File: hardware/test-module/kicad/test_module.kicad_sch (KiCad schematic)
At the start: 14 parts, among them J1 Barrel_Jack_12V, M1 ERM_Motor, M2 Stepper_4wire, M3 Servo_3pin, U1 D24V22F5_Buck, U2 Pi_Pico_W, U3 DRV2605L_Breakout, U4 DRV8871_Breakout, U5 Tic_T500

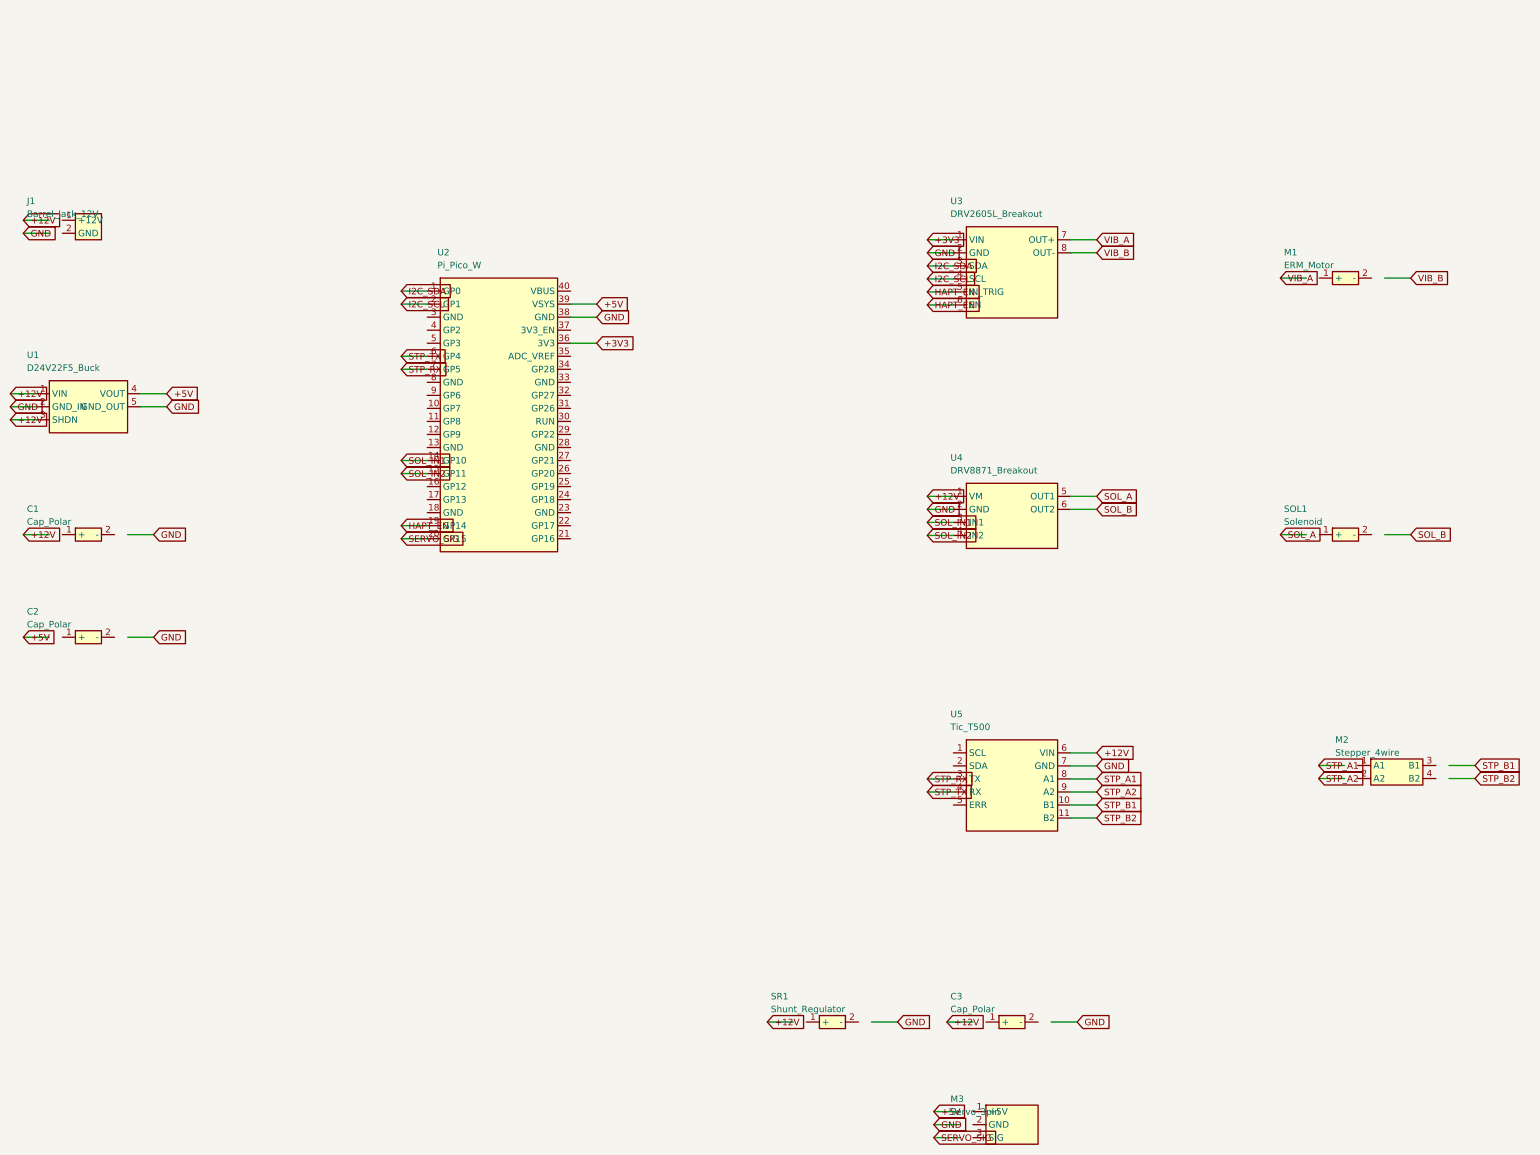
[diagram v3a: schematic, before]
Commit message: Add dual-servo dispensing-angle control (unison, mirrored) to firmware + schematic
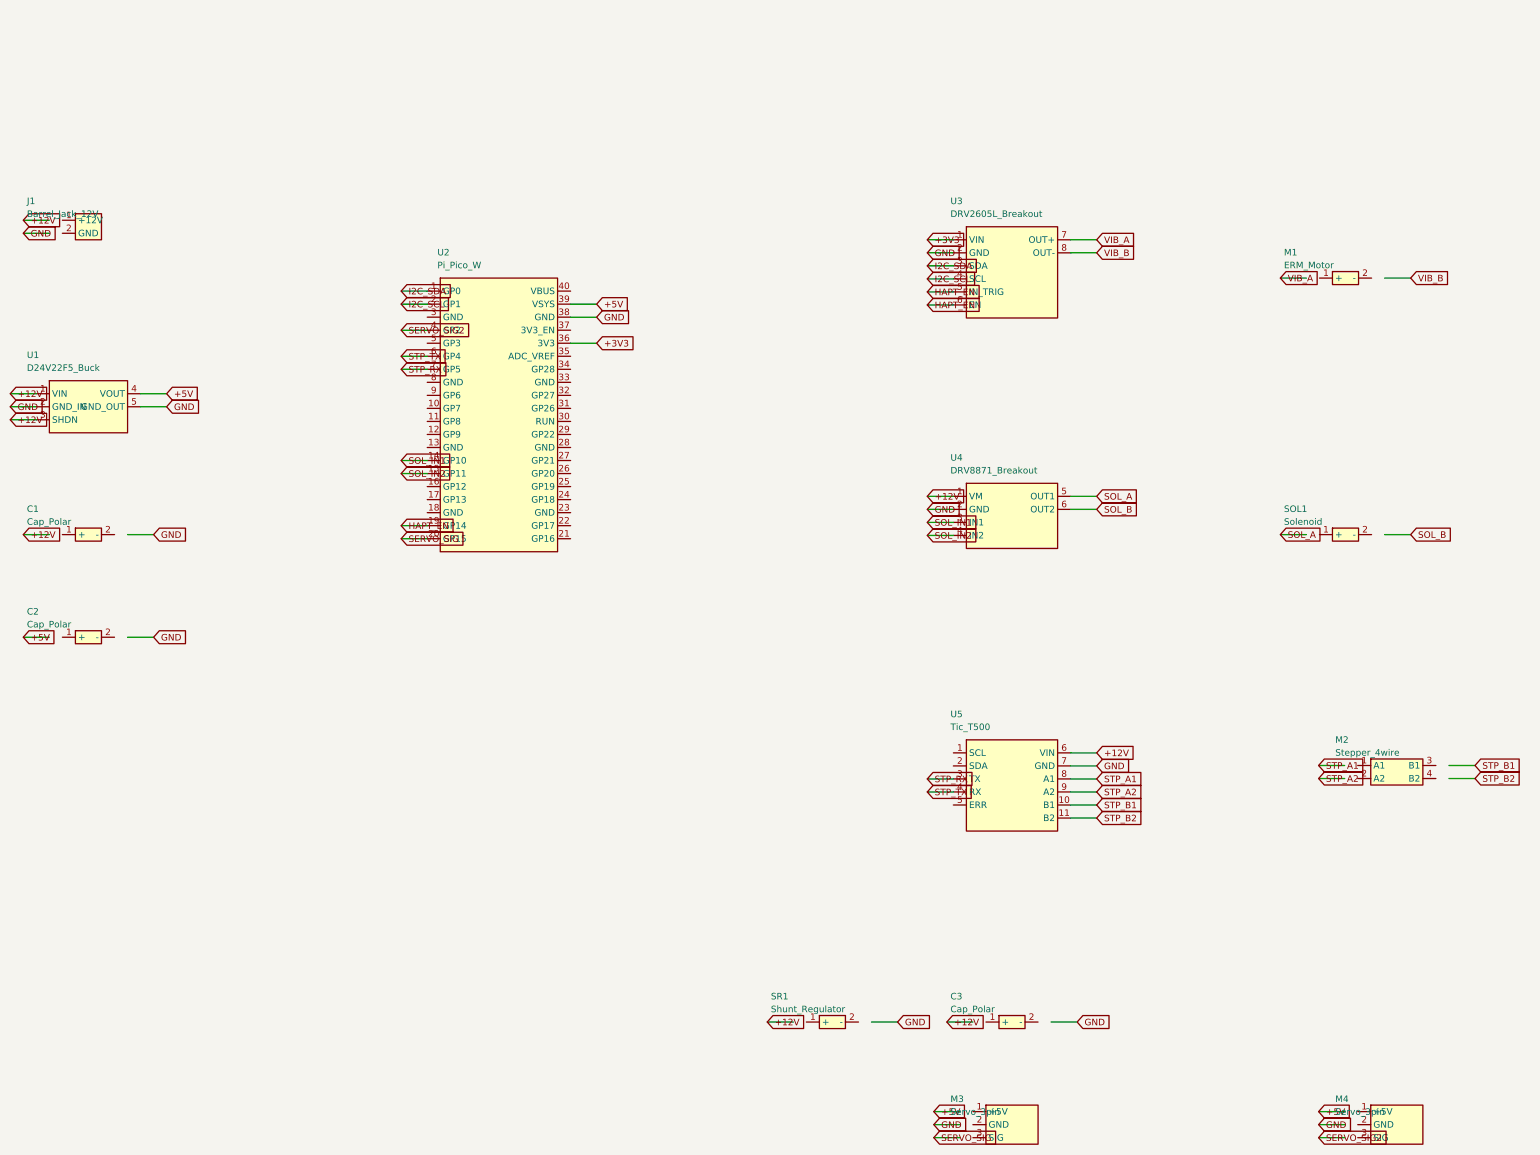
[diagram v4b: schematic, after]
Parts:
- added M4: Servo_3pin, symbol test_module:Servo_3pin
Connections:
- net SERVO_SIG2: now reaches U2.4 (GP2)
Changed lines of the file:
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@@
+  (effects (font (size 1.27 1.27)) (justify left))
+)
+(wire (pts (xy 96.03 60.16) (xy 90.95 60.16))
+  (stroke (width 0) (type default)) (stroke (width 0) (type default))
+)
+(global_label "SERVO_SIG2" (shape input) (at 90.95 60.16 180) (fields_autoplaced)
   (effects (font (size 1.27 1.27)) (justify left))
 )
@@
   (effects (font (size 1.27 1.27)) (justify left))
 )
+(symbol (lib_id "test_module:Servo_3pin") (at 285 215 0) (unit 1)
+  (in_bom yes) (on_board yes) (dnp no)
+  (property "Reference" "M4" (id 0) (at 273 210 0)
+    (effects (font (size 1.27 1.27)) (justify left)))
+  (property "Value" "Servo_3pin" (id 1) (at 273 212.5 0)
+    (effects (font (size 1.27 1.27)) (justify left)))
+  (property "Footprint" "" (id 2) (at 285 215 0)
+    (effects (font (size 1.27 1.27)) hide))
+  (property "Datasheet" "" (id 3) (at 285 215 0)
+    (effects (font (size 1.27 1.27)) hide))
+  (instances
+    (project "test_module"
+      (path "/00000000-0000-0000-0002-000000000001"
+        (reference "M4") (unit 1)
+      )
+    )
+  )
+)
+(wire (pts (xy 274.84 212.46) (xy 269.76 212.46))
+  (stroke (width 0) (type default)) (stroke (width 0) (type default))
+)
+(global_label "+5V" (shape input) (at 269.76 212.46 180) (fields_autoplaced)
+  (effects (font (size 1.27 1.27)) (justify left))
+)
+(wire (pts (xy 274.84 215) (xy 269.76 215))
+  (stroke (width 0) (type default)) (stroke (width 0) (type default))
+)
+(global_label "GND" (shape input) (at 269.76 215 180) (fields_autoplaced)
+  (effects (font (size 1.27 1.27)) (justify left))
+)
+(wire (pts (xy 274.84 217.54) (xy 269.76 217.54))
+  (stroke (width 0) (type default)) (stroke (width 0) (type default))
+)
+(global_label "SERVO_SIG2" (shape input) (at 269.76 217.54 180) (fields_autoplaced)
+  (effects (font (size 1.27 1.27)) (justify left))
+)
